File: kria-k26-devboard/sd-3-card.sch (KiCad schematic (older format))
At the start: 23 parts, among them J2 1140084168, Q1 BSS123, Q2 AO3401A, U4 NVT4858HKZ, U5 TPS2116DRLR

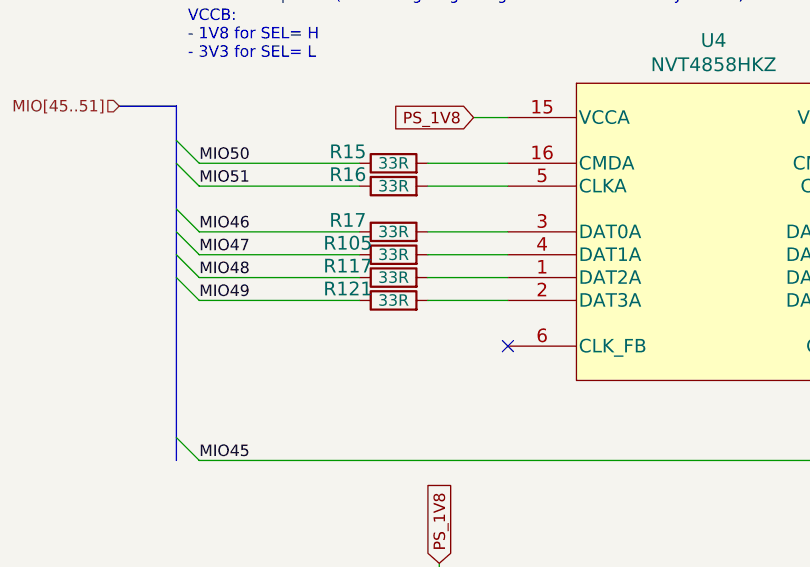
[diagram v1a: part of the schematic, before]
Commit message: Fixed possible FTDI-USB backfeeding issue, finished PS and FTDI power planes creation, finished routing of FTDI/Debug part
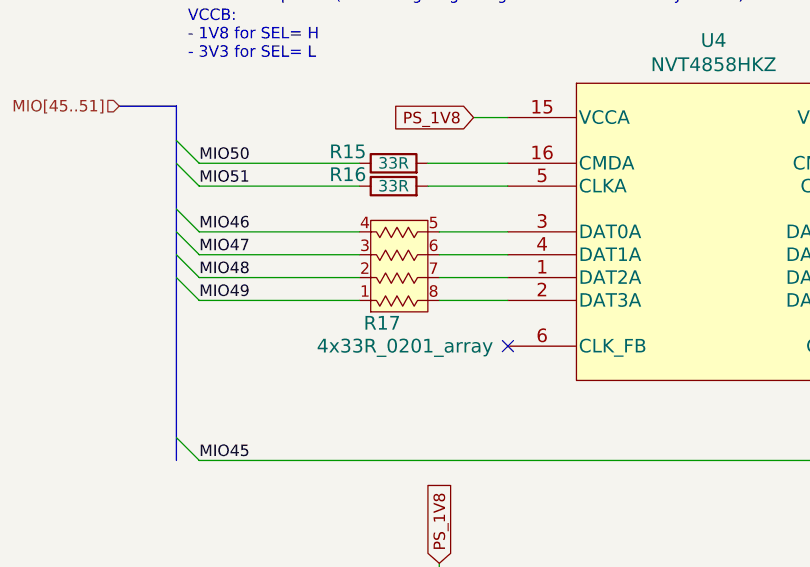
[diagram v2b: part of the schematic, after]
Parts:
- removed R105, R117, R121, R17: R_33R_0402, antmicro-footprints:0402-res, symbol antmicroResistors0402:R_33R_0402
- added R17: 4x33R_0201_array, antmicro-footprints:EXB18V, symbol antmicroResistorNetworksArrays:4x33R_0201_array
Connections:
- net MIO46: now also R17.4
- net MIO47: now also R17.3
- net MIO48: now also R17.2
- net MIO49: now also R17.1
- net at U4.1 (DAT2A): now also R17.7
- net at U4.2 (DAT3A): now also R17.8
- net at U4.3 (DAT0A): now also R17.5
- net at U4.4 (DAT1A): now also R17.6
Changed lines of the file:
@@
 Wire Wire Line
 	3550 4500 3700 4500
-Wire Wire Line
-	3350 5000 3700 5000
-Wire Wire Line
-	3700 5100 3350 5100
-Wire Wire Line
-	3350 5200 3700 5200
-Wire Wire Line
-	3700 5300 3350 5300
 $Comp
 L antmicroResistors0402:R_33R_0402 R16
@@
 Wire Wire Line
 	5950 6750 5950 6800
-$Comp
-L antmicroResistors0402:R_33R_0402 R17
-U 1 1 6B9BC7A8
-P 3200 5000
-F 0 "R17" H 3000 5050 60  0000 C CNN
-F 1 "R_33R_0402" H 3200 4850 60  0001 C CNN
-F 2 "antmicro-footprints:0402-res" H 3400 5200 60  0001 L CNN
-F 3 "" H 3200 5000 50  0001 C CNN
-F 4 "Vishay" H 3400 5400 60  0001 L CNN "Manufacturer"
-F 5 "CRCW040233R0FKED" H 3400 5300 60  0001 L CNN "MPN"
-F 6 "33R" H 3200 5000 50  0000 C CNN "Val"
-	1    3200 5000
-	1    0    0    -1
-$EndComp
-$Comp
-L antmicroResistors0402:R_33R_0402 R105
-U 1 1 6B9BCD69
-P 3200 5100
-F 0 "R105" H 3000 5150 60  0000 C CNN
-F 1 "R_33R_0402" H 3200 4950 60  0001 C CNN
-F 2 "antmicro-footprints:0402-res" H 3400 5300 60  0001 L CNN
-F 3 "" H 3200 5100 50  0001 C CNN
-F 4 "Vishay" H 3400 5500 60  0001 L CNN "Manufacturer"
-F 5 "CRCW040233R0FKED" H 3400 5400 60  0001 L CNN "MPN"
-F 6 "33R" H 3200 5100 50  0000 C CNN "Val"
-	1    3200 5100
-	1    0    0    -1
-$EndComp
-$Comp
-L antmicroResistors0402:R_33R_0402 R117
-U 1 1 6B9BD877
-P 3200 5200
-F 0 "R117" H 3000 5250 60  0000 C CNN
-F 1 "R_33R_0402" H 3200 5050 60  0001 C CNN
-F 2 "antmicro-footprints:0402-res" H 3400 5400 60  0001 L CNN
-F 3 "" H 3200 5200 50  0001 C CNN
-F 4 "Vishay" H 3400 5600 60  0001 L CNN "Manufacturer"
-F 5 "CRCW040233R0FKED" H 3400 5500 60  0001 L CNN "MPN"
-F 6 "33R" H 3200 5200 50  0000 C CNN "Val"
-	1    3200 5200
-	1    0    0    -1
-$EndComp
-$Comp
-L antmicroResistors0402:R_33R_0402 R121
-U 1 1 6B9BDB94
-P 3200 5300
-F 0 "R121" H 3000 5350 60  0000 C CNN
-F 1 "R_33R_0402" H 3200 5150 60  0001 C CNN
-F 2 "antmicro-footprints:0402-res" H 3400 5500 60  0001 L CNN
-F 3 "" H 3200 5300 50  0001 C CNN
-F 4 "Vishay" H 3400 5700 60  0001 L CNN "Manufacturer"
-F 5 "CRCW040233R0FKED" H 3400 5600 60  0001 L CNN "MPN"
-F 6 "33R" H 3200 5300 50  0000 C CNN "Val"
-	1    3200 5300
-	1    0    0    -1
-$EndComp
 Text Label 5700 5300 0    50   ~ 0
 SD_DAT3
@@
 Text Label 5700 4800 0    50   ~ 0
 SD_CLK
+$Comp
+L antmicroResistorNetworksArrays:4x33R_0201_array R17
+U 1 1 632D3168
+P 3250 4900
+F 0 "R17" H 3150 5400 60  0000 C CNN
+F 1 "4x33R_0201_array" H 3250 5500 60  0000 C CNN
+F 2 "antmicro-footprints:EXB18V" H 3050 5650 60  0001 L CNN
+F 3 "http://industrial.panasonic.com/cdbs/www-data/pdf/AOC0000/AOC0000C14.pdf" H 3050 5650 60  0001 L CNN
+F 4 "EXB-18V330JX" H 3050 5850 60  0001 L CNN "MPN"
+F 5 "Panasonic" H 3050 5750 60  0001 L CNN "Manufacturer"
+	1    3250 4900
+	1    0    0    1
+$EndComp
+Wire Wire Line
+	3400 5000 3700 5000
+Wire Wire Line
+	3400 5100 3700 5100
+Wire Wire Line
+	3400 5200 3700 5200
+Wire Wire Line
+	3400 5300 3700 5300
 Wire Bus Line
 	2250 4450 2250 6000

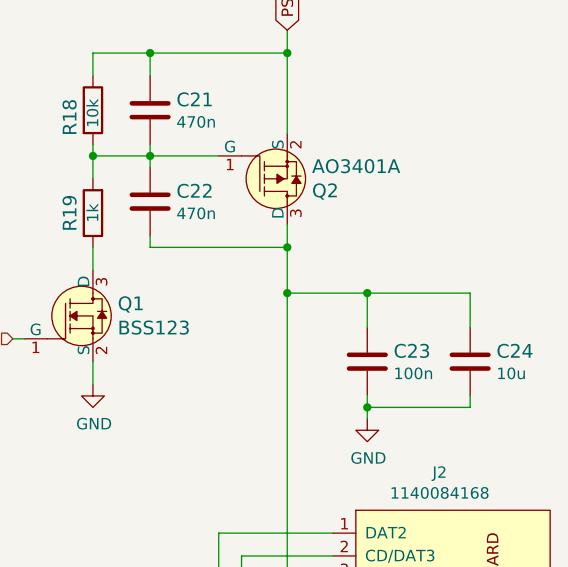
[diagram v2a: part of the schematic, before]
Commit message: Optimization of power planes, fixed missing capacitors on USB 3.0, unify shields, polishing of layout
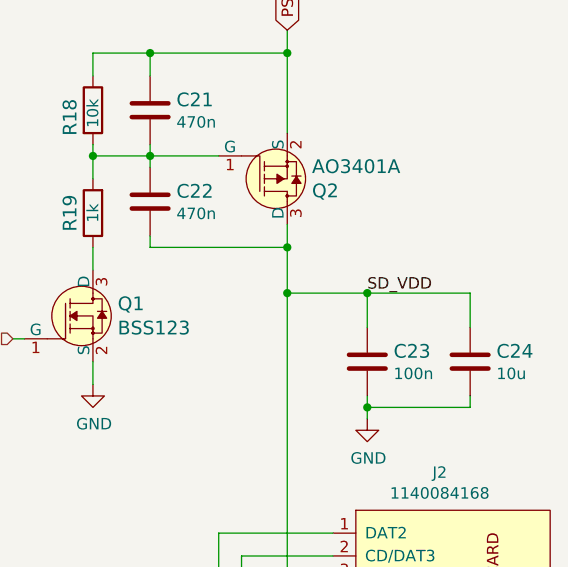
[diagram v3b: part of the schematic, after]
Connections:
- net SD_VDD: now reaches C22.2, C23.1, C24.1, J2.4 (VDD), Q2.3 (D)
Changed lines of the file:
@@
 Wire Bus Line
 	2250 4450 2250 6000
+Text Label 8900 3350 0    50   ~ 0
+SD_VDD
 $EndSCHEMATC

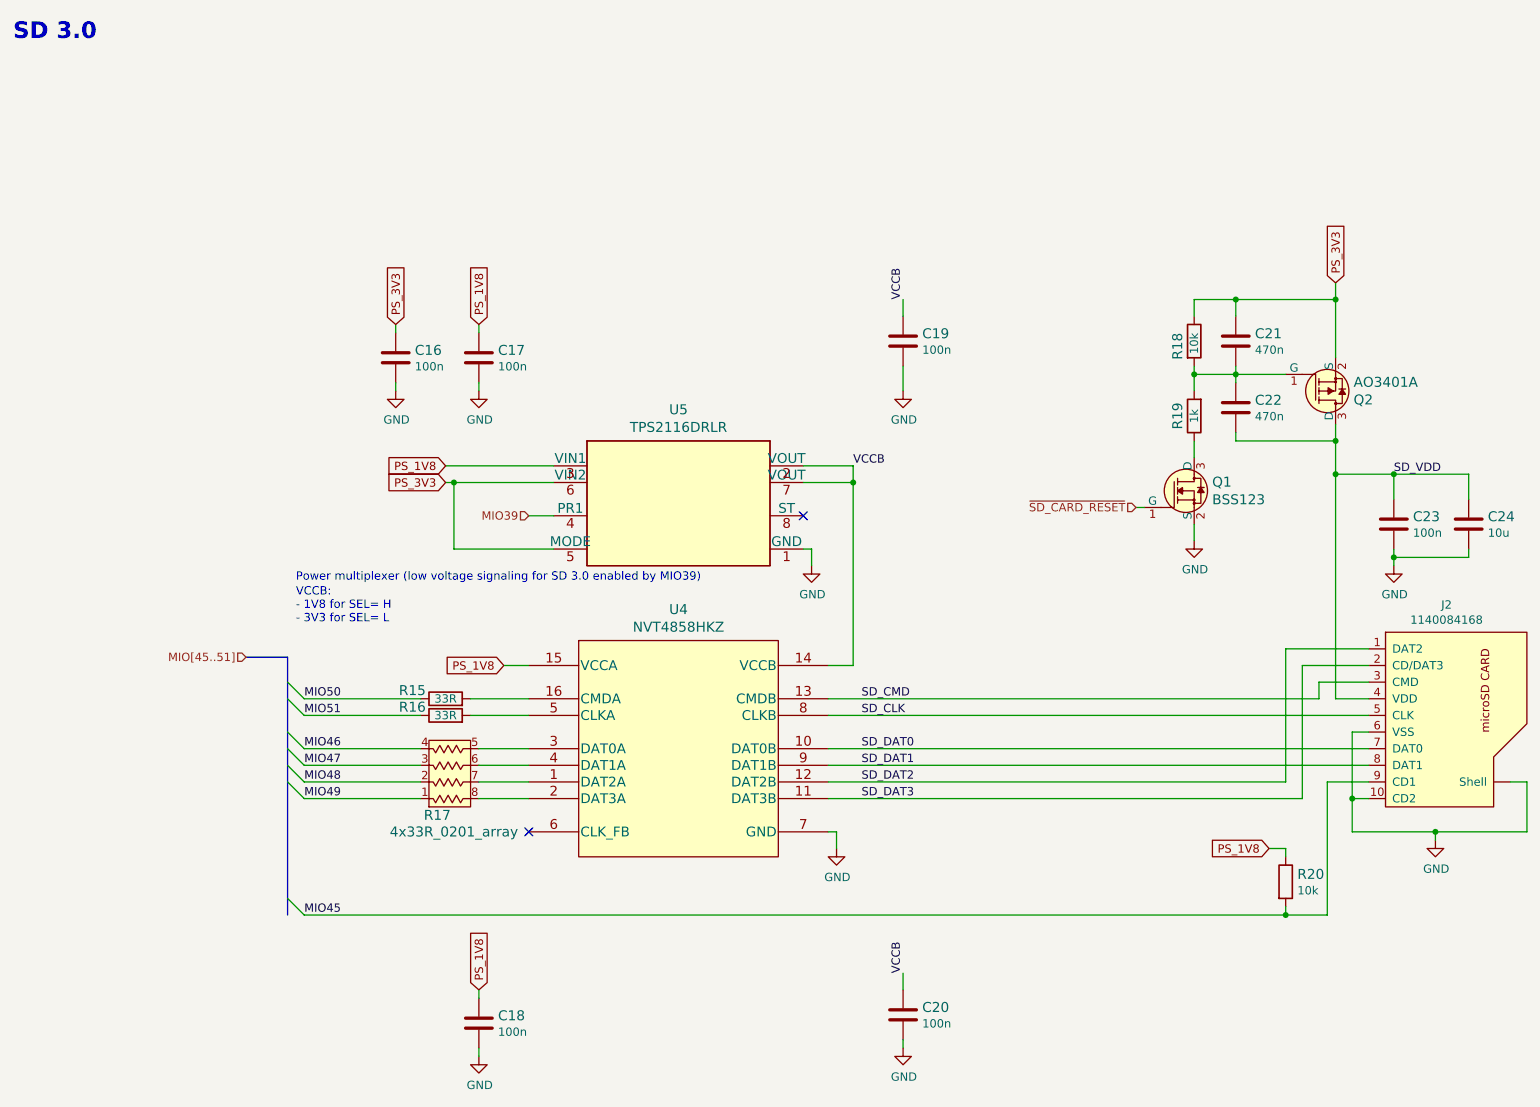
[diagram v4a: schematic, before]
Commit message: Fixed missing USB - M2 connection, finishing touches of PCB
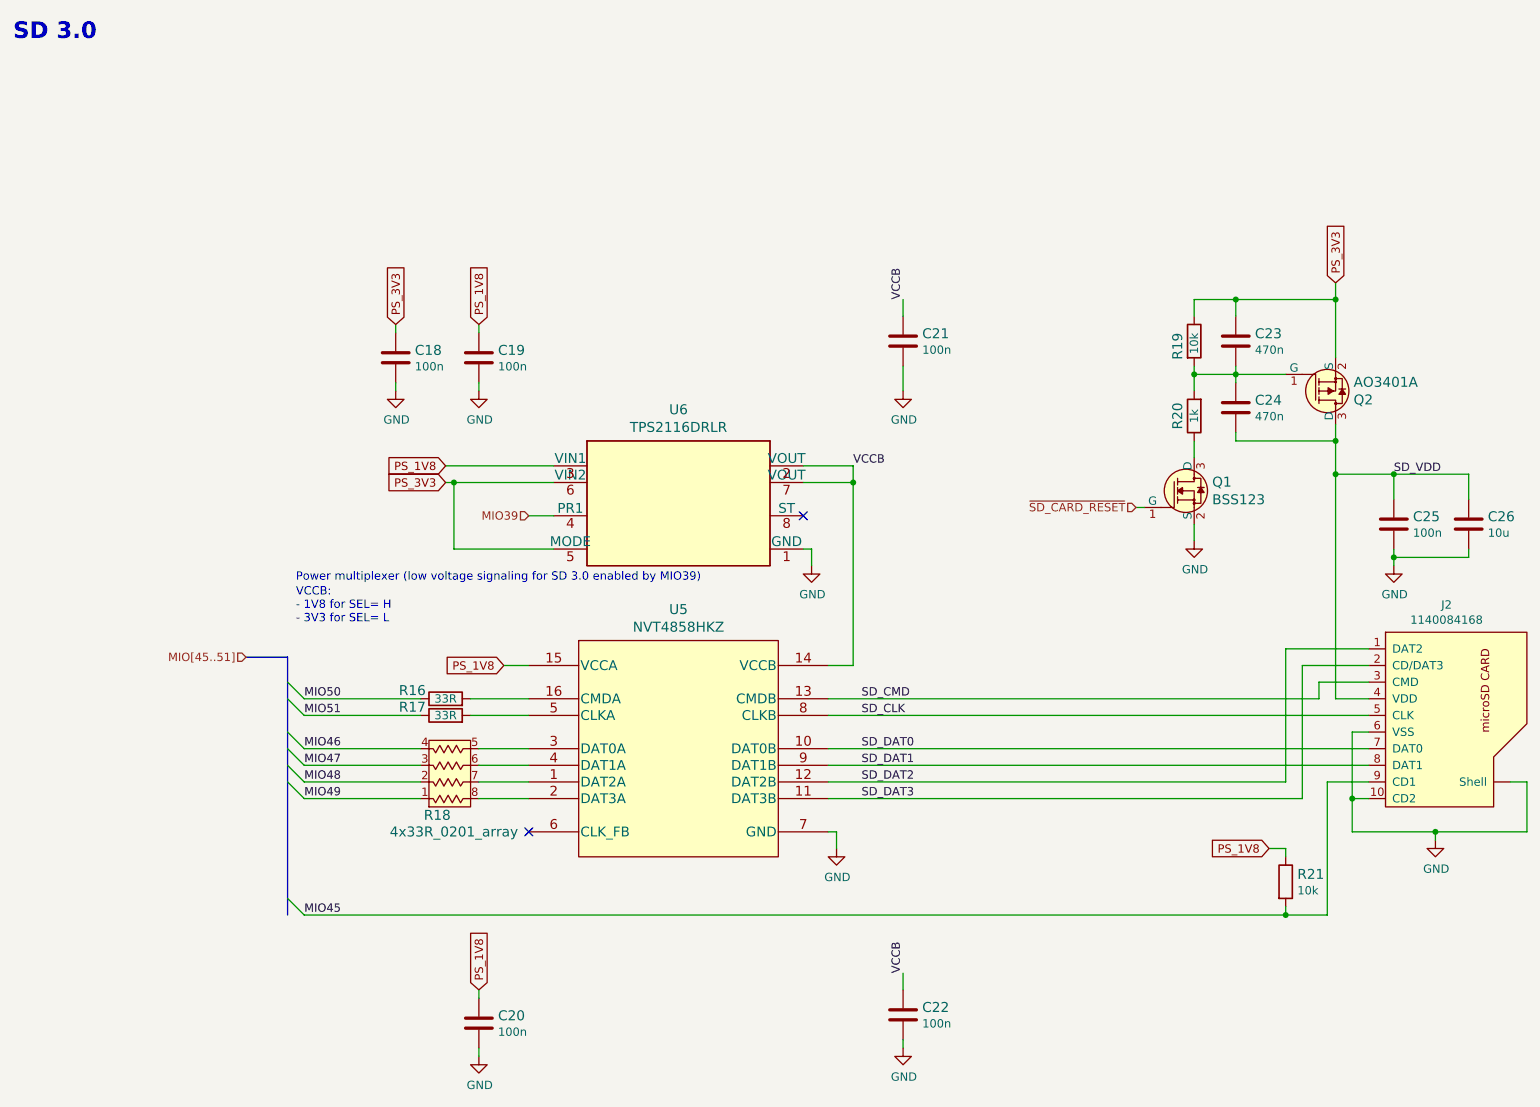
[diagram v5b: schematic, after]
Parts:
- renumbered C16 to C18, C17 to C19, C18 to C20, C19 to C21, C20 to C22, C21 to C23, C22 to C24, C23 to C25, C24 to C26, R15 to R16, R16 to R17, R17 to R18, R18 to R19, R19 to R20, R20 to R21, U4 to U5, U5 to U6
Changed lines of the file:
@@
 $EndDescr
 $Comp
-L antmicroLogicTranslatorsLevelShifters:NVT4858HKZ U4
+L antmicroLogicTranslatorsLevelShifters:NVT4858HKZ U5
 U 1 1 630B0AC4
 P 3700 4550
-F 0 "U4" H 4600 4937 60  0000 C CNN
+F 0 "U5" H 4600 4937 60  0000 C CNN
 F 1 "NVT4858HKZ" H 4600 4831 60  0000 C CNN
 F 2 "antmicro-footprints:SOT1161-2" H 4600 4790 60  0001 C CNN
@@
 Connection ~ 5650 3400
 $Comp
-L power:GND #PWR029
+L power:GND #PWR032
 U 1 1 631D2E7A
 P 5400 3900
-F 0 "#PWR029" H 5400 3650 50  0001 C CNN
+F 0 "#PWR032" H 5400 3650 50  0001 C CNN
 F 1 "GND" H 5405 3727 50  0000 C CNN
 F 2 "" H 5400 3900 50  0001 C CNN
@@
 	3200 3400 3250 3400
 $Comp
-L antmicroPMICPowerDistributionSwitchesLoadDrivers:TPS2116DRLR U5
+L antmicroPMICPowerDistributionSwitchesLoadDrivers:TPS2116DRLR U6
 U 1 1 631CFC7A
 P 3850 3300
-F 0 "U5" H 4600 3638 60  0000 C CNN
+F 0 "U6" H 4600 3638 60  0000 C CNN
 F 1 "TPS2116DRLR" H 4600 3532 60  0000 C CNN
 F 2 "antmicro-footprints:Texas_DRL0008A" H 4300 2600 60  0001 C CNN
@@
 	3550 4500 3700 4500
 $Comp
-L antmicroResistors0402:R_33R_0402 R16
+L antmicroResistors0402:R_33R_0402 R17
 U 1 1 631DF31D
 P 3200 4800
-F 0 "R16" H 3000 4850 60  0000 C CNN
+F 0 "R17" H 3000 4850 60  0000 C CNN
 F 1 "R_33R_0402" H 3200 4650 60  0001 C CNN
 F 2 "antmicro-footprints:0402-res" H 3400 5000 60  0001 L CNN
@@
 $EndComp
 $Comp
-L antmicroResistors0402:R_33R_0402 R15
+L antmicroResistors0402:R_33R_0402 R16
 U 1 1 631E087B
 P 3200 4700
-F 0 "R15" H 3000 4750 60  0000 C CNN
+F 0 "R16" H 3000 4750 60  0000 C CNN
 F 1 "R_33R_0402" H 3200 4550 60  0001 C CNN
 F 2 "antmicro-footprints:0402-res" H 3400 4900 60  0001 L CNN
@@
 	8450 4600 8750 4600
 $Comp
-L power:GND #PWR030
+L power:GND #PWR033
 U 1 1 631E6AA8
 P 5550 5600
-F 0 "#PWR030" H 5550 5350 50  0001 C CNN
+F 0 "#PWR033" H 5550 5350 50  0001 C CNN
 F 1 "GND" H 5555 5427 50  0000 C CNN
 F 2 "" H 5550 5600 50  0001 C CNN
@@
 PS_3V3
 $Comp
-L antmicroCapacitors0402:C_100n_0402 C16
+L antmicroCapacitors0402:C_100n_0402 C18
 U 1 1 631F0D3B
 P 2900 2650
-F 0 "C16" H 3015 2695 60  0000 L CNN
+F 0 "C18" H 3015 2695 60  0000 L CNN
 F 1 "C_100n_0402" H 2900 2500 60  0001 C CNN
 F 2 "antmicro-footprints:0402-cap" H 3100 2850 60  0001 L CNN
@@
 $EndComp
 $Comp
-L antmicroCapacitors0402:C_100n_0402 C17
+L antmicroCapacitors0402:C_100n_0402 C19
 U 1 1 631F1104
 P 3400 2650
-F 0 "C17" H 3515 2695 60  0000 L CNN
+F 0 "C19" H 3515 2695 60  0000 L CNN
 F 1 "C_100n_0402" H 3400 2500 60  0001 C CNN
 F 2 "antmicro-footprints:0402-cap" H 3600 2850 60  0001 L CNN
@@
 $EndComp
 $Comp
-L antmicroCapacitors0402:C_100n_0402 C19
+L antmicroCapacitors0402:C_100n_0402 C21
 U 1 1 631F1457
 P 5950 2550
-F 0 "C19" H 6065 2595 60  0000 L CNN
+F 0 "C21" H 6065 2595 60  0000 L CNN
 F 1 "C_100n_0402" H 5950 2400 60  0001 C CNN
 F 2 "antmicro-footprints:0402-cap" H 6150 2750 60  0001 L CNN
@@
 	3400 2500 3400 2450
 $Comp
-L power:GND #PWR026
+L power:GND #PWR029
 U 1 1 63200563
 P 2900 2850
-F 0 "#PWR026" H 2900 2600 50  0001 C CNN
+F 0 "#PWR029" H 2900 2600 50  0001 C CNN
 F 1 "GND" H 2905 2677 50  0000 C CNN
 F 2 "" H 2900 2850 50  0001 C CNN
@@
 MIO39
 $Comp
-L antmicroCapacitors0402:C_100n_0402 C23
+L antmicroCapacitors0402:C_100n_0402 C25
 U 1 1 6323158C
 P 8900 3650
-F 0 "C23" H 9015 3695 60  0000 L CNN
+F 0 "C25" H 9015 3695 60  0000 L CNN
 F 1 "C_100n_0402" H 8900 3500 60  0001 C CNN
 F 2 "antmicro-footprints:0402-cap" H 9100 3850 60  0001 L CNN
@@
 	8900 3900 8900 3850
 $Comp
-L antmicroCapacitors0603:C_10u_0603 C24
+L antmicroCapacitors0603:C_10u_0603 C26
 U 1 1 632347EF
 P 9350 3650
-F 0 "C24" H 9465 3695 60  0000 L CNN
+F 0 "C26" H 9465 3695 60  0000 L CNN
 F 1 "C_10u_0603" H 9350 3500 60  0001 C CNN
 F 2 "antmicro-footprints:0603-cap" H 9550 3850 60  0001 L CNN
@@
 Connection ~ 8900 3350
 $Comp
-L power:GND #PWR034
+L power:GND #PWR037
 U 1 1 632316CE
 P 8900 3900
-F 0 "#PWR034" H 8900 3650 50  0001 C CNN
+F 0 "#PWR037" H 8900 3650 50  0001 C CNN
 F 1 "GND" H 8905 3727 50  0000 C CNN
 F 2 "" H 8900 3900 50  0001 C CNN
@@
 	5950 2400 5950 2300
 $Comp
-L power:GND #PWR027
+L power:GND #PWR030
 U 1 1 63203F42
 P 3400 2850
-F 0 "#PWR027" H 3400 2600 50  0001 C CNN
+F 0 "#PWR030" H 3400 2600 50  0001 C CNN
 F 1 "GND" H 3405 2677 50  0000 C CNN
 F 2 "" H 3400 2850 50  0001 C CNN
@@
 $EndComp
 $Comp
-L power:GND #PWR031
+L power:GND #PWR034
 U 1 1 63278518
 P 5950 2850
-F 0 "#PWR031" H 5950 2600 50  0001 C CNN
+F 0 "#PWR034" H 5950 2600 50  0001 C CNN
 F 1 "GND" H 5955 2677 50  0000 C CNN
 F 2 "" H 5950 2850 50  0001 C CNN
@@
 	9700 5500 9150 5500
 $Comp
-L power:GND #PWR035
+L power:GND #PWR038
 U 1 1 632822AB
 P 9150 5550
-F 0 "#PWR035" H 9150 5300 50  0001 C CNN
+F 0 "#PWR038" H 9150 5300 50  0001 C CNN
 F 1 "GND" H 9155 5377 50  0000 C CNN
 F 2 "" H 9150 5550 50  0001 C CNN
@@
 $EndComp
 $Comp
-L power:GND #PWR033
+L power:GND #PWR036
 U 1 1 66661087
 P 7700 3750
-F 0 "#PWR033" H 7700 3500 50  0001 C CNN
+F 0 "#PWR036" H 7700 3500 50  0001 C CNN
 F 1 "GND" H 7705 3577 50  0000 C CNN
 F 2 "" H 7700 3750 50  0001 C CNN
@@
 	7700 2300 7700 2400
 $Comp
-L antmicroResistors0402:R_1k_0402 R19
+L antmicroResistors0402:R_1k_0402 R20
 U 1 1 66639BBE
 P 7700 3000
-F 0 "R19" H 7700 3100 60  0000 C CNN
+F 0 "R20" H 7700 3100 60  0000 C CNN
 F 1 "R_1k_0402" H 7700 2850 60  0001 C CNN
 F 2 "antmicro-footprints:0402-res" H 7900 3200 60  0001 L CNN
@@
 $EndComp
 $Comp
-L antmicroCapacitors0402:C_470n_0402 C21
+L antmicroCapacitors0402:C_470n_0402 C23
 U 1 1 666642E9
 P 7950 2550
-F 0 "C21" H 8065 2595 60  0000 L CNN
+F 0 "C23" H 8065 2595 60  0000 L CNN
 F 1 "C_470n_0402" H 7950 2400 60  0001 C CNN
 F 2 "antmicro-footprints:0402-cap" H 8150 2750 60  0001 L CNN
@@
 $EndComp
 $Comp
-L antmicroResistors0402:R_10k_0402 R18
+L antmicroResistors0402:R_10k_0402 R19
 U 1 1 6667AA59
 P 7700 2550
-F 0 "R18" H 7650 2450 60  0000 L CNN
+F 0 "R19" H 7650 2450 60  0000 L CNN
 F 1 "R_10k_0402" H 7700 2400 60  0001 C CNN
 F 2 "antmicro-footprints:0402-res" H 7900 2750 60  0001 L CNN
@@
 ~SD_CARD_RESET
 $Comp
-L antmicroCapacitors0402:C_470n_0402 C22
+L antmicroCapacitors0402:C_470n_0402 C24
 U 1 1 667B7A84
 P 7950 2950
-F 0 "C22" H 8065 2995 60  0000 L CNN
+F 0 "C24" H 8065 2995 60  0000 L CNN
 F 1 "C_470n_0402" H 7950 2800 60  0001 C CNN
 F 2 "antmicro-footprints:0402-cap" H 8150 3150 60  0001 L CNN
@@
 	8550 2300 8550 2650
 $Comp
-L antmicroResistors0402:R_10k_0402 R20
+L antmicroResistors0402:R_10k_0402 R21
 U 1 1 63286775
 P 8250 5800
-F 0 "R20" V 8205 5870 60  0000 L CNN
+F 0 "R21" V 8205 5870 60  0000 L CNN
 F 1 "R_10k_0402" H 8250 5650 60  0001 C CNN
 F 2 "antmicro-footprints:0402-res" H 8450 6000 60  0001 L CNN
@@
 PS_1V8
 $Comp
-L antmicroCapacitors0402:C_100n_0402 C18
+L antmicroCapacitors0402:C_100n_0402 C20
 U 1 1 6986927B
 P 3400 6650
-F 0 "C18" H 3515 6695 60  0000 L CNN
+F 0 "C20" H 3515 6695 60  0000 L CNN
 F 1 "C_100n_0402" H 3400 6500 60  0001 C CNN
 F 2 "antmicro-footprints:0402-cap" H 3600 6850 60  0001 L CNN
@@
 	3400 6850 3400 6800
 $Comp
-L power:GND #PWR028
+L power:GND #PWR031
 U 1 1 69869287
 P 3400 6850
-F 0 "#PWR028" H 3400 6600 50  0001 C CNN
+F 0 "#PWR031" H 3400 6600 50  0001 C CNN
 F 1 "GND" H 3405 6677 50  0000 C CNN
 F 2 "" H 3400 6850 50  0001 C CNN
@@
 $EndComp
 $Comp
-L antmicroCapacitors0402:C_100n_0402 C20
+L antmicroCapacitors0402:C_100n_0402 C22
 U 1 1 69871ED9
 P 5950 6600
-F 0 "C20" H 6065 6645 60  0000 L CNN
+F 0 "C22" H 6065 6645 60  0000 L CNN
 F 1 "C_100n_0402" H 5950 6450 60  0001 C CNN
 F 2 "antmicro-footprints:0402-cap" H 6150 6800 60  0001 L CNN
@@
 	5950 6450 5950 6350
 $Comp
-L power:GND #PWR032
+L power:GND #PWR035
 U 1 1 6987213A
 P 5950 6800
-F 0 "#PWR032" H 5950 6550 50  0001 C CNN
+F 0 "#PWR035" H 5950 6550 50  0001 C CNN
 F 1 "GND" H 5955 6627 50  0000 C CNN
 F 2 "" H 5950 6800 50  0001 C CNN
@@
 SD_CLK
 $Comp
-L antmicroResistorNetworksArrays:4x33R_0201_array R17
+L antmicroResistorNetworksArrays:4x33R_0201_array R18
 U 1 1 632D3168
 P 3250 4900
-F 0 "R17" H 3150 5400 60  0000 C CNN
+F 0 "R18" H 3150 5400 60  0000 C CNN
 F 1 "4x33R_0201_array" H 3250 5500 60  0000 C CNN
 F 2 "antmicro-footprints:EXB18V" H 3050 5650 60  0001 L CNN
